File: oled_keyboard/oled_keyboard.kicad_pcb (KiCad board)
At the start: 4 copper layers, 100 x 100 mm, 127 parts, among them J1 Conn_01x20_Socket, J10 Conn_01x20_Socket, J11 Conn_01x20_Socket, J12 Conn_01x20_Socket, J2 Conn_01x20_Socket, J3 Conn_01x20_Socket, J4 Conn_01x20_Socket, J5 Conn_01x20_Socket, J6 Conn_01x20_Socket, J7 Conn_01x20_Socket, J8 Conn_01x20_Socket, J9 Conn_01x20_Socket, SW1 SW_Push, SW10 SW_Push, SW11 SW_Push, SW12 SW_Push, SW2 SW_Push, SW3 SW_Push, SW4 SW_Push, SW5 SW_Push, SW6 SW_Push, SW7 SW_Push, SW8 SW_Push, SW9 SW_Push, U1 TPS61088RHLR

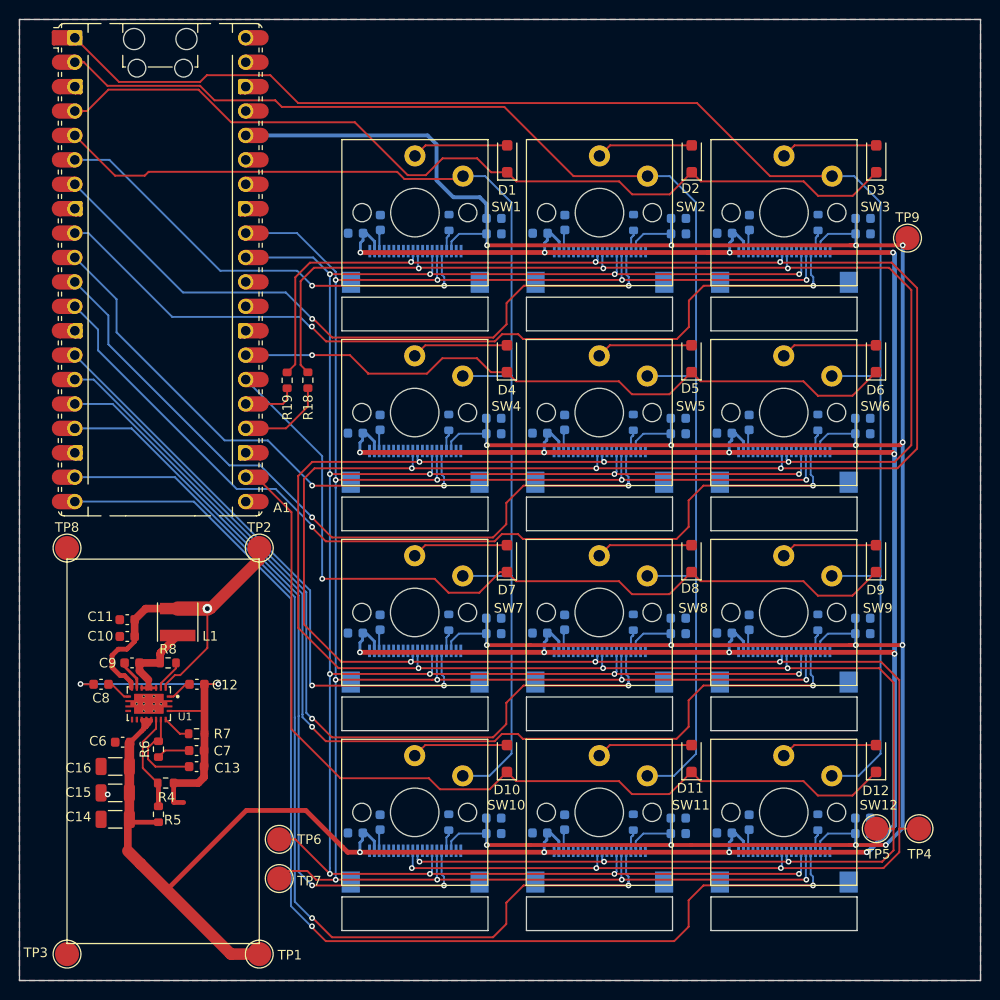
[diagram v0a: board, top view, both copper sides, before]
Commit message: feat: changed fpc connectors
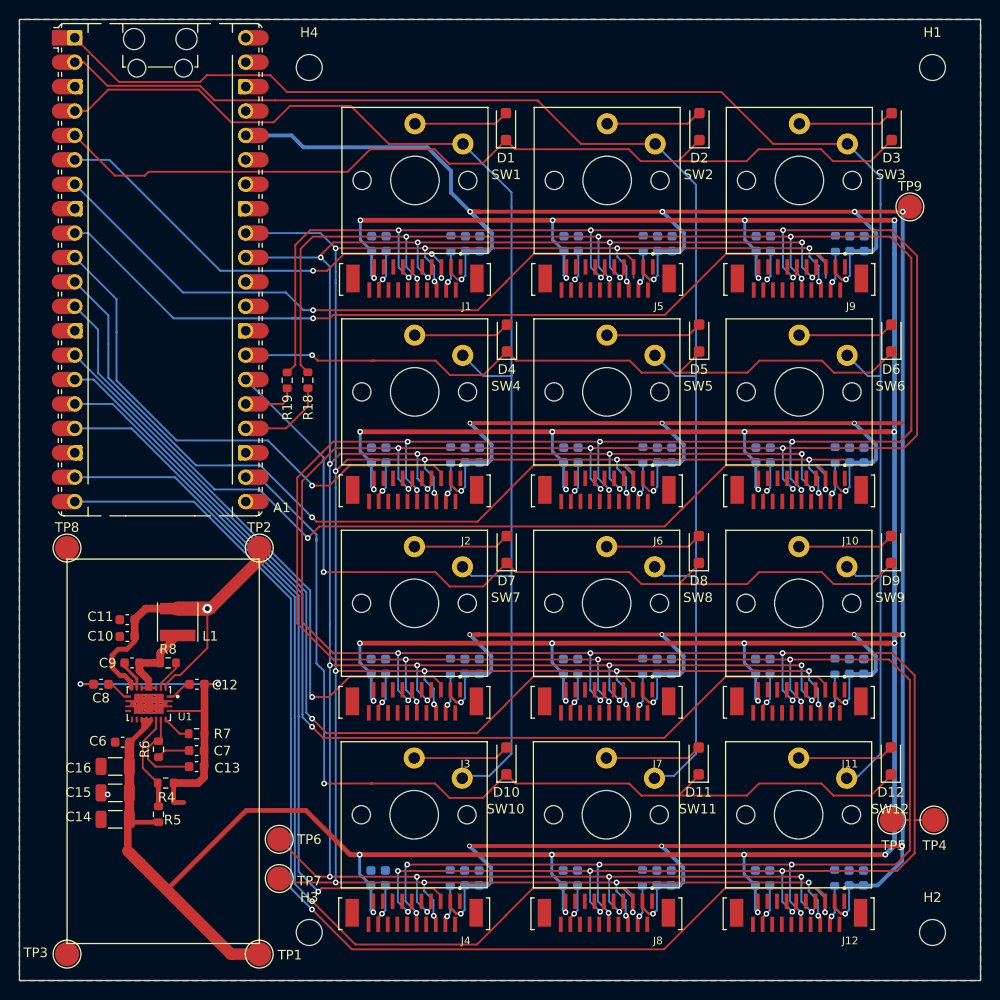
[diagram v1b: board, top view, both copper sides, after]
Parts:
- added H1: MountingHole, MountingHole:MountingHole_2.7mm_M2.5, F.Cu at (176.8, 35.5)
- added H2: MountingHole, MountingHole:MountingHole_2.7mm_M2.5, F.Cu at (176.8, 125.5)
- added H3: MountingHole, MountingHole:MountingHole_2.7mm_M2.5, F.Cu at (112.0, 125.5)
- added H4: MountingHole, MountingHole:MountingHole_2.7mm_M2.5, F.Cu at (112.0, 35.5)
- J1, J12, J4, J8: footprint 20pin_connector:HRS_TF31-20S-0.5SH_800_ -> 20pin_conn_vert:TE_2-1734742-0; moved to F.Cu
- J10, J11, J2, J3, J5, J6, J7, J9: footprint 20p_connector:HRS_TF31-20S-0.5SH_800_ -> 20pin_conn_vert:TE_2-1734742-0; moved to F.Cu
- moved C21 6.92 mm to (128.2, 119.8), turned to 90 degrees
- moved C31 6.61 mm to (148.2, 119.8), turned to 90 degrees
- moved C47 6.23 mm to (169.7, 119.8), turned to 90 degrees
- moved C55 6.18 mm to (159.9, 119.8)
- moved R17 6.06 mm to (166.7, 119.8)
- moved C39 5.95 mm to (139.9, 119.8)
- moved R13 5.88 mm to (146.7, 119.8)
- moved C25 5.83 mm to (119.9, 119.8)
- moved R9 5.80 mm to (126.7, 119.8)
- moved C59 5.68 mm to (158.4, 119.8), turned to 90 degrees
- moved C43 5.27 mm to (138.4, 119.8), turned to 90 degrees
- moved C26 5.24 mm to (129.7, 97.8), turned to 90 degrees
- moved C50 5.09 mm to (159.9, 97.8)
- moved C42 5.07 mm to (149.7, 97.8), turned to 90 degrees
- moved C58 5.03 mm to (169.7, 97.8), turned to 90 degrees
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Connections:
- A1 pad 4: /ROW1 -> /COL1
- A1 pad 5: /COL1 -> /ROW1
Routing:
- net 3V3: track 361.9 -> 455.2 mm, vias 16 -> 26
- net /SCLK: track 323.9 -> 399.6 mm, vias 12 -> 24
- net /SDIN: track 327.7 -> 393.6 mm, vias 12 -> 24
- net /RES: track 313.1 -> 358.8 mm, vias 16 -> 32
- net /DC: track 303.9 -> 340.8 mm, vias 16 -> 28
- net VCC: track 407.9 -> 444.2 mm, vias 16 -> 28
- net /ROW4: track 97.0 -> 103.1 mm, vias 0 -> 1
- net /COL1: track 122.5 -> 128.1 mm
- net Net-(J8-Pin_18): track 1.89 -> 5.83 mm, vias 0 -> 1
- net Net-(J12-Pin_18): track 1.89 -> 5.83 mm, vias 0 -> 1
- net Net-(J3-Pin_18): track 1.89 -> 5.83 mm, vias 0 -> 1
- net Net-(J4-Pin_18): track 1.89 -> 5.83 mm, vias 0 -> 1
- net Net-(J2-Pin_18): track 1.89 -> 5.83 mm, vias 0 -> 1
- net Net-(J7-Pin_18): track 1.89 -> 5.83 mm, vias 0 -> 1
- net Net-(J11-Pin_18): track 1.89 -> 5.83 mm, vias 0 -> 1
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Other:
- outline, holes or cut-outs redrawn
- board text added: "J10"
- board text added: "J11"
- board text added: "J12"
- board text added: "J2"
- board text added: "J3"
- board text added: "J6"
- board text added: "J7"
- board text added: "J9"

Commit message: release v4.0
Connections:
- A1 pad 37: GND -> unconnected-(A1-3V3_EN-Pad37)
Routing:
- net 3V3: track 455.2 -> 431.8 mm, vias 26 -> 27
- net /RES: track 358.8 -> 345.8 mm, vias 32 -> 28
- net /SCLK: track 399.6 -> 392.7 mm
- net /CS3: track 89.1 -> 84.9 mm
- net VCC: track 444.2 -> 448.3 mm
- net /DC: track 340.8 -> 343.4 mm
- net /CS1: track 46.7 -> 44.6 mm, vias 3 -> 1
- net /SDIN: track 393.6 -> 395.7 mm
- net /CS2: track 68.1 -> 66.3 mm
- net Net-(J8-Pin_18): track 5.83 -> 4.56 mm
- net Net-(J6-Pin_18): track 3.29 -> 4.56 mm
- net Net-(J3-Pin_18): track 5.83 -> 4.56 mm
- net Net-(J12-Pin_18): track 5.83 -> 4.56 mm
- net Net-(J10-Pin_18): track 3.29 -> 4.56 mm
- net Net-(J9-Pin_18): track 3.29 -> 4.56 mm
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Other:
- board text added: "oled keyboard v4.0 by Xin 2026.7.15"
- board text removed: "J12"
- board text removed: "J9"
- board text removed: "oled keyboard v3.1 by Xin 2026.6.23"

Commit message: release v5.2
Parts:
- removed TP4, TP5: TestPoint, TestPoint:TestPoint_Pad_D2.5mm
- added C60: 0.1uF, Capacitor_SMD:C_0603_1608Metric, B.Cu at (125.4, 52.3)
- added C61: 0.1uF, Capacitor_SMD:C_0603_1608Metric, B.Cu at (125.5, 74.3)
- added C62: 0.1uF, Capacitor_SMD:C_0603_1608Metric, B.Cu at (125.4, 96.3)
- added C63: 0.1uF, Capacitor_SMD:C_0603_1608Metric, B.Cu at (125.4, 118.2)
- added C64: 0.1uF, Capacitor_SMD:C_0603_1608Metric, B.Cu at (145.5, 52.3)
- added C65: 0.1uF, Capacitor_SMD:C_0603_1608Metric, B.Cu at (145.5, 74.3)
- added C66: 0.1uF, Capacitor_SMD:C_0603_1608Metric, B.Cu at (145.5, 96.3)
- added C67: 0.1uF, Capacitor_SMD:C_0603_1608Metric, B.Cu at (145.5, 118.2)
- added C68: 0.1uF, Capacitor_SMD:C_0603_1608Metric, B.Cu at (165.6, 118.2)
- added C69: 0.1uF, Capacitor_SMD:C_0603_1608Metric, B.Cu at (165.6, 96.3)
- added C70: 0.1uF, Capacitor_SMD:C_0603_1608Metric, B.Cu at (165.6, 74.3)
- added C71: 0.1uF, Capacitor_SMD:C_0603_1608Metric, B.Cu at (165.6, 52.2)
- added R20: 10K, Resistor_SMD:R_0603_1608Metric, B.Cu at (131.4, 52.3)
- added R21: 10K, Resistor_SMD:R_0603_1608Metric, B.Cu at (151.5, 52.3)
- added R22: 10K, Resistor_SMD:R_0603_1608Metric, B.Cu at (171.5, 52.3)
- added R23: 10K, Resistor_SMD:R_0603_1608Metric, B.Cu at (131.4, 74.3)
- added R24: 10K, Resistor_SMD:R_0603_1608Metric, B.Cu at (151.5, 74.3)
- added R25: 10K, Resistor_SMD:R_0603_1608Metric, B.Cu at (171.5, 74.3)
- added R26: 10K, Resistor_SMD:R_0603_1608Metric, B.Cu at (131.4, 96.3)
- added R27: 10K, Resistor_SMD:R_0603_1608Metric, B.Cu at (151.5, 96.3)
- added R28: 10K, Resistor_SMD:R_0603_1608Metric, B.Cu at (171.5, 96.3)
- added R29: 10K, Resistor_SMD:R_0603_1608Metric, B.Cu at (131.4, 118.3)
- added R30: 10K, Resistor_SMD:R_0603_1608Metric, B.Cu at (151.5, 118.3)
- added R31: 10K, Resistor_SMD:R_0603_1608Metric, B.Cu at (171.5, 118.3)
- moved H1 91.0 mm to (177.8, 126.5)
- moved H2 91.0 mm to (177.8, 34.5)
- moved TP9 63.7 mm to (111.1, 43.6)
- moved TP6 63.3 mm to (114.1, 52.7)
- moved TP7 62.7 mm to (171.2, 126.9)
- moved C51 6.53 mm to (174.5, 118.3)
- moved C41 6.41 mm to (154.4, 74.3)
- moved C40 6.39 mm to (154.4, 52.3)
- moved D12 5.97 mm to (178.4, 106.7)
- moved D9 5.95 mm to (178.4, 84.7)
- moved D6 5.92 mm to (178.4, 62.7)
- moved D11 5.91 mm to (158.4, 106.7)
- moved D1 5.90 mm to (138.3, 40.7)
- moved D3 5.90 mm to (178.4, 40.7)
- moved D8 5.89 mm to (158.4, 84.7)
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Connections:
- A1 pad 31: /DC -> /RES
- A1 pad 32: /RES -> /DC
- J1 pad 1: unconnected-(J1-Pin_1-Pad1) -> GND
- J1 pad 2: unconnected-(J1-Pin_2-Pad2) -> GND
- J1 pad 20: unconnected-(J1-Pin_20-Pad20) -> GND
- J10 pad 1: unconnected-(J10-Pin_1-Pad1) -> GND
- J10 pad 2: unconnected-(J10-Pin_2-Pad2) -> GND
- J10 pad 20: unconnected-(J10-Pin_20-Pad20) -> GND
- J11 pad 1: unconnected-(J11-Pin_1-Pad1) -> GND
- J11 pad 2: unconnected-(J11-Pin_2-Pad2) -> GND
- J11 pad 20: unconnected-(J11-Pin_20-Pad20) -> GND
- J12 pad 1: unconnected-(J12-Pin_1-Pad1) -> GND
- J12 pad 2: unconnected-(J12-Pin_2-Pad2) -> GND
- J12 pad 20: unconnected-(J12-Pin_20-Pad20) -> GND
- J2 pad 1: unconnected-(J2-Pin_1-Pad1) -> GND
- J2 pad 2: unconnected-(J2-Pin_2-Pad2) -> GND
- J2 pad 20: unconnected-(J2-Pin_20-Pad20) -> GND
- J3 pad 1: unconnected-(J3-Pin_1-Pad1) -> GND
- J3 pad 2: unconnected-(J3-Pin_2-Pad2) -> GND
- J3 pad 20: unconnected-(J3-Pin_20-Pad20) -> GND
- J4 pad 1: unconnected-(J4-Pin_1-Pad1) -> GND
- J4 pad 2: unconnected-(J4-Pin_2-Pad2) -> GND
- J4 pad 20: unconnected-(J4-Pin_20-Pad20) -> GND
- J5 pad 1: unconnected-(J5-Pin_1-Pad1) -> GND
- J5 pad 2: unconnected-(J5-Pin_2-Pad2) -> GND
- J5 pad 20: unconnected-(J5-Pin_20-Pad20) -> GND
- J6 pad 1: unconnected-(J6-Pin_1-Pad1) -> GND
- J6 pad 2: unconnected-(J6-Pin_2-Pad2) -> GND
- J6 pad 20: unconnected-(J6-Pin_20-Pad20) -> GND
- J7 pad 1: unconnected-(J7-Pin_1-Pad1) -> GND
- J7 pad 2: unconnected-(J7-Pin_2-Pad2) -> GND
- J7 pad 20: unconnected-(J7-Pin_20-Pad20) -> GND
- J8 pad 1: unconnected-(J8-Pin_1-Pad1) -> GND
- J8 pad 2: unconnected-(J8-Pin_2-Pad2) -> GND
- J8 pad 20: unconnected-(J8-Pin_20-Pad20) -> GND
- J9 pad 1: unconnected-(J9-Pin_1-Pad1) -> GND
- J9 pad 2: unconnected-(J9-Pin_2-Pad2) -> GND
- J9 pad 20: unconnected-(J9-Pin_20-Pad20) -> GND
- R18 pad 1: /SCLK -> /SCK
- R18 pad 2: /SCK -> /SCLK
- R19 pad 1: /SDIN -> /MOSI
- R19 pad 2: /MOSI -> /SDIN
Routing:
- net GND: track 0.00 -> 102.5 mm, vias 1 -> 106
- net 3V3: track 431.8 -> 372.8 mm, vias 27 -> 28
- net /SCLK: track 392.7 -> 343.8 mm, vias 24 -> 0
- net /SDIN: track 395.7 -> 354.6 mm, vias 24 -> 0
- net /RES: track 345.8 -> 323.1 mm, vias 28 -> 27
- net VCC: track 448.3 -> 431.4 mm, vias 28 -> 33
- net /CS3: track 84.9 -> 100.8 mm, vias 1 -> 4
- net /CS2: track 66.3 -> 81.9 mm, vias 1 -> 4
- net /CS9: track 102.9 -> 117.7 mm, vias 1 -> 4
- net /CS8: track 83.4 -> 97.5 mm, vias 1 -> 4
- net /CS7: track 60.4 -> 74.4 mm, vias 1 -> 2
- net /CS6: track 94.2 -> 107.6 mm, vias 1 -> 4
- net /DC: track 343.4 -> 331.4 mm
- net /CS5: track 75.0 -> 86.8 mm, vias 1 -> 4
- net /CS1: track 44.6 -> 54.7 mm, vias 1 -> 2
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- added copper zone on In2.Cu, net VCC
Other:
- board text added: "oled keyboard v5.2 by Xin 2026.9.15"
- board text removed: "oled keyboard v4.0 by Xin 2026.7.15"
